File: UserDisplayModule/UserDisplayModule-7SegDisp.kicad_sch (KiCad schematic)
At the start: 15 parts, among them U4 74HC595

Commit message: doubled LEDs + started PCB
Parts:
- removed D13: 1SEG7, symbol Device:LED
- removed D14: 1SEG6, symbol Device:LED
- removed D15: 1SEG5, symbol Device:LED
- removed D16: 1SEG4, symbol Device:LED
- removed D17: 1SEG3, symbol Device:LED
- removed D18: 1SEG2, symbol Device:LED
- removed D19: 1SEG1, symbol Device:LED
- added D27: SEG7, LED_SMD:LED_0805_2012Metric, symbol Device:LED
- added D28, D30, D32, D34, D36, D38, D40: BAT1, LED_SMD:LED_0805_2012Metric, symbol Device:LED
- added D29: SEG6, LED_SMD:LED_0805_2012Metric, symbol Device:LED
- added D31: SEG5, LED_SMD:LED_0805_2012Metric, symbol Device:LED
- added D33: SEG4, LED_SMD:LED_0805_2012Metric, symbol Device:LED
- added D35: SEG3, LED_SMD:LED_0805_2012Metric, symbol Device:LED
- added D37: SEG2, LED_SMD:LED_0805_2012Metric, symbol Device:LED
- added D39: SEG1, LED_SMD:LED_0805_2012Metric, symbol Device:LED
- R13, R14, R15, R16, R17, R18, R19: footprint (none) -> Resistor_SMD:R_0805_2012Metric
- U4: footprint (none) -> ImportedFootprints:CD74HC595E
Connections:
- net GND: now also D28.1 (K), D30.1 (K), D32.1 (K), D34.1 (K), D36.1 (K), D38.1 (K), D40.1 (K)
- net at R14.2: now also D29.2 (A)
- net at R13.2: now also D27.2 (A)
- net at R15.2: now also D31.2 (A)
- net at R19.2: now also D39.2 (A)
- net at R16.2: now also D33.2 (A)
- net at R18.2: now also D37.2 (A)
- net at R17.2: now also D35.2 (A)
- new net: D29.1 (K), D30.2 (A)
- new net: D31.1 (K), D32.2 (A)
- new net: D37.1 (K), D38.2 (A)
- new net: D27.1 (K), D28.2 (A)
- new net: D39.1 (K), D40.2 (A)
- new net: D35.1 (K), D36.2 (A)
- new net: D33.1 (K), D34.2 (A)
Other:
- note added: "7-Segment Display"
- moved on the sheet: R13, R14, R15, R16, R17, R18, R19

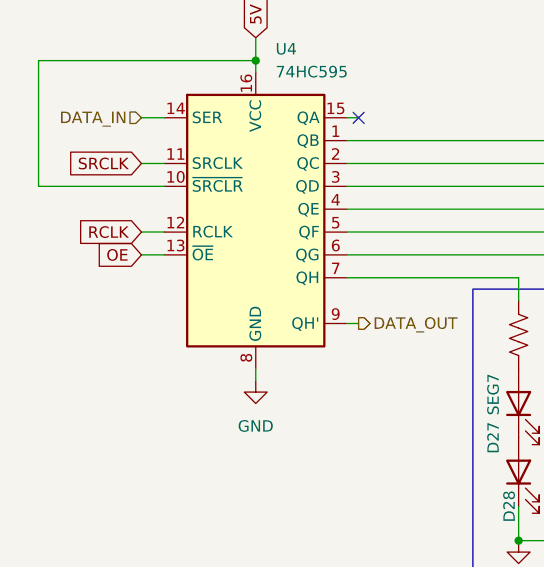
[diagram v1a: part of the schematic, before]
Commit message: finished routing pcb (minus ground pour)
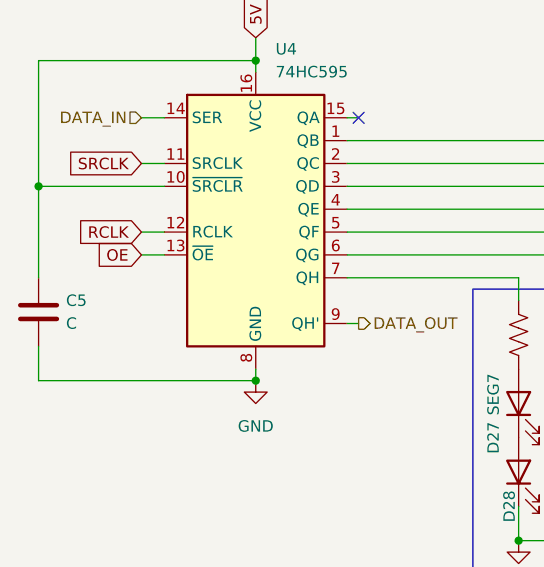
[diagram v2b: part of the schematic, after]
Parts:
- added C5: C, Capacitor_SMD:C_0805_2012Metric, symbol Device:C
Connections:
- net 5V: now also C5.1
- net GND: now also C5.2
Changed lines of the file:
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@@
+	)
+	(junction
+		(at 78.74 62.23)
+		(diameter 0)
+		(color 0 0 0 0)
 	)
 	(junction
@@
 	)
 	(junction
+		(at 102.87 83.82)
+		(diameter 0)
+		(color 0 0 0 0)
+	)
+	(junction
 		(at 132.08 101.6)
 		(diameter 0)
@@
 	(wire
 		(pts
+			(xy 78.74 62.23) (xy 78.74 72.39)
+		)
+		(stroke
+			(width 0)
+			(type default)
+		)
+	)
+	(wire
+		(pts
 			(xy 113.03 54.61) (xy 114.3 54.61)
 		)
@@
 	(wire
 		(pts
+			(xy 78.74 83.82) (xy 102.87 83.82)
+		)
+		(stroke
+			(width 0)
+			(type default)
+		)
+	)
+	(wire
+		(pts
 			(xy 113.03 62.23) (xy 187.96 62.23)
 		)
@@
 		(pts
 			(xy 113.03 57.15) (xy 215.9 57.15)
+		)
+		(stroke
+			(width 0)
+			(type default)
+		)
+	)
+	(wire
+		(pts
+			(xy 78.74 80.01) (xy 78.74 83.82)
 		)
 		(stroke
@@
 					(unit 1)
 				)
+			)
+		)
+	)
+	(symbol
+		(lib_id "Device:C")
+		(at 78.74 76.2 0)
+		(unit 1)
+		(exclude_from_sim no)
+		(in_bom yes)
+		(on_board yes)
+		(dnp no)
+		(property "Reference" "C5"
+			(at 81.788 74.93 0)
+			(effects
+				(font
+					(size 1.27 1.27)
+				)
+				(justify left)
+			)
+		)
+		(property "Value" "C"
+			(at 81.788 77.47 0)
+			(effects
+				(font
+					(size 1.27 1.27)
+				)
+				(justify left)
+			)
+		)
+		(property "Footprint" "Capacitor_SMD:C_0805_2012Metric"
+			(at 79.7052 80.01 0)
+			(effects
+				(font
+					(size 1.27 1.27)
+				)
+				(hide yes)
+			)
+		)
+		(property "Datasheet" "~"
+			(at 78.74 76.2 0)
+			(effects
+				(font
+					(size 1.27 1.27)
+				)
+				(hide yes)
+			)
+		)
+		(property "Description" "Unpolarized capacitor"
+			(at 78.74 76.2 0)
+			(effects
+				(font
+					(size 1.27 1.27)
+				)
+				(hide yes)
+			)
+		)
+		(pin "2"
+		)
+		(pin "1"
+		)
+		(instances
+			(project "UserDisplayModule"
+				(path "/352d7abe-fc72-4473-8b68-62eecf44f496/0028eded-db04-4ec8-8943-95ff11960fa1"
+					(reference "C5")
+					(unit 1)
+				)
+				(path "/352d7abe-fc72-4473-8b68-62eecf44f496/d2d9e71a-442b-4090-b915-11a66e8f5c2a"
+					(reference "C6")
+					(unit 1)
+				)
+				(path "/352d7abe-fc72-4473-8b68-62eecf44f496/9650799d-9072-4dba-8139-3ec1f2ecacfb"
+					(reference "C7")
+					(unit 1)
+				)
+				(path "/352d7abe-fc72-4473-8b68-62eecf44f496/b2dcfe67-b35c-4587-a29d-880113cdb577"
+					(reference "C8")
+					(unit 1)
+				)

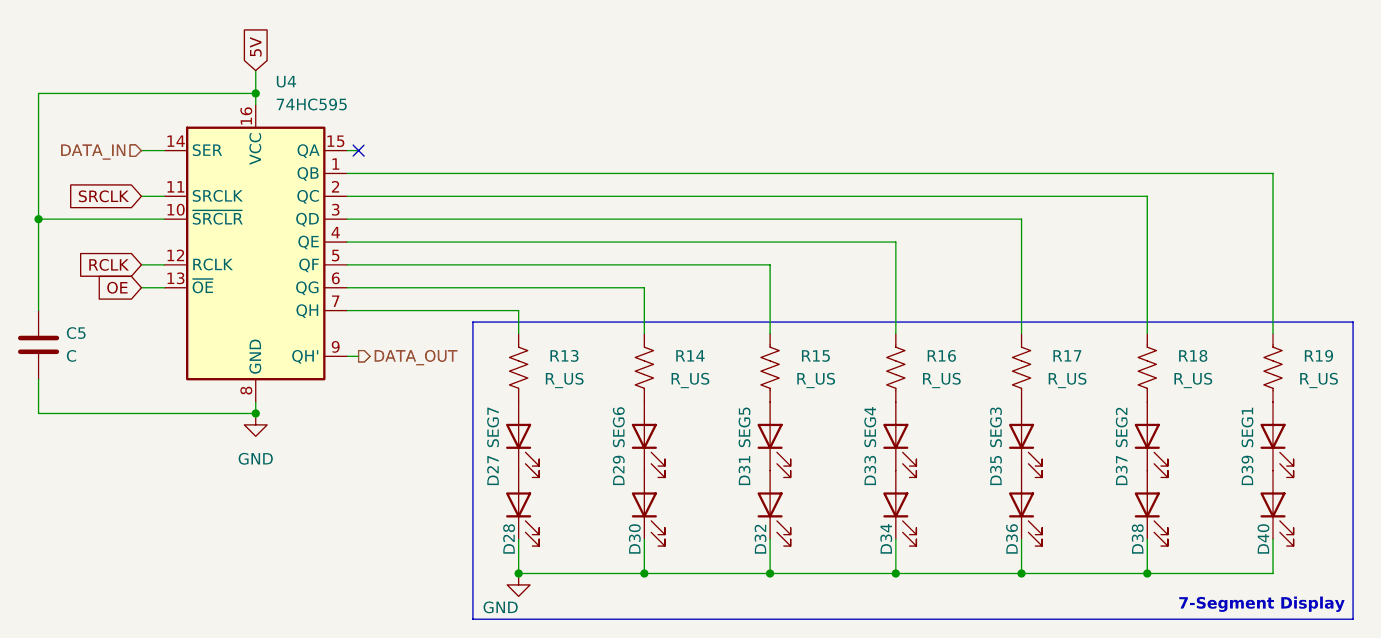
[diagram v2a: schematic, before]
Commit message: added 3d models, fixed footprints, finished routing
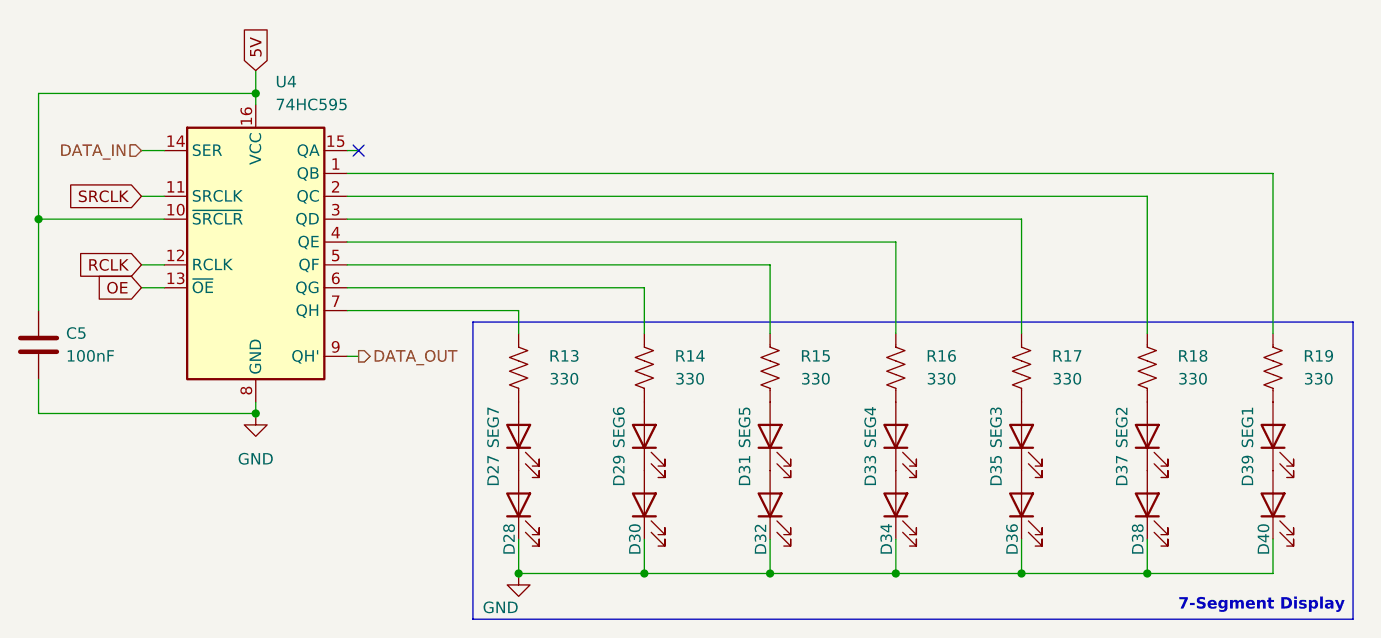
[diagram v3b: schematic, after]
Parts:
- C5: value C -> 100nF
- R13, R14, R15, R16, R17, R18, R19: value R_US -> 330
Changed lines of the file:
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@@
 			)
 		)
-		(property "Value" "R_US"
+		(property "Value" "330"
 			(at 151.13 80.01 0)
 			(effects
@@
 			)
 		)
-		(property "Value" "R_US"
+		(property "Value" "330"
 			(at 137.16 80.01 0)
 			(effects
@@
 			)
 		)
-		(property "Value" "R_US"
+		(property "Value" "330"
 			(at 165.1 80.01 0)
 			(effects
@@
 			)
 		)
-		(property "Value" "R_US"
+		(property "Value" "330"
 			(at 220.98 80.01 0)
 			(effects
@@
 			)
 		)
-		(property "Value" "R_US"
+		(property "Value" "330"
 			(at 179.07 80.01 0)
 			(effects
@@
 			)
 		)
-		(property "Value" "R_US"
+		(property "Value" "330"
 			(at 207.01 80.01 0)
 			(effects
@@
 			)
 		)
-		(property "Value" "R_US"
+		(property "Value" "330"
 			(at 193.04 80.01 0)
 			(effects
@@
 			)
 		)
-		(property "Value" "C"
+		(property "Value" "100nF"
 			(at 81.788 77.47 0)
 			(effects

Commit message: added digikey pns
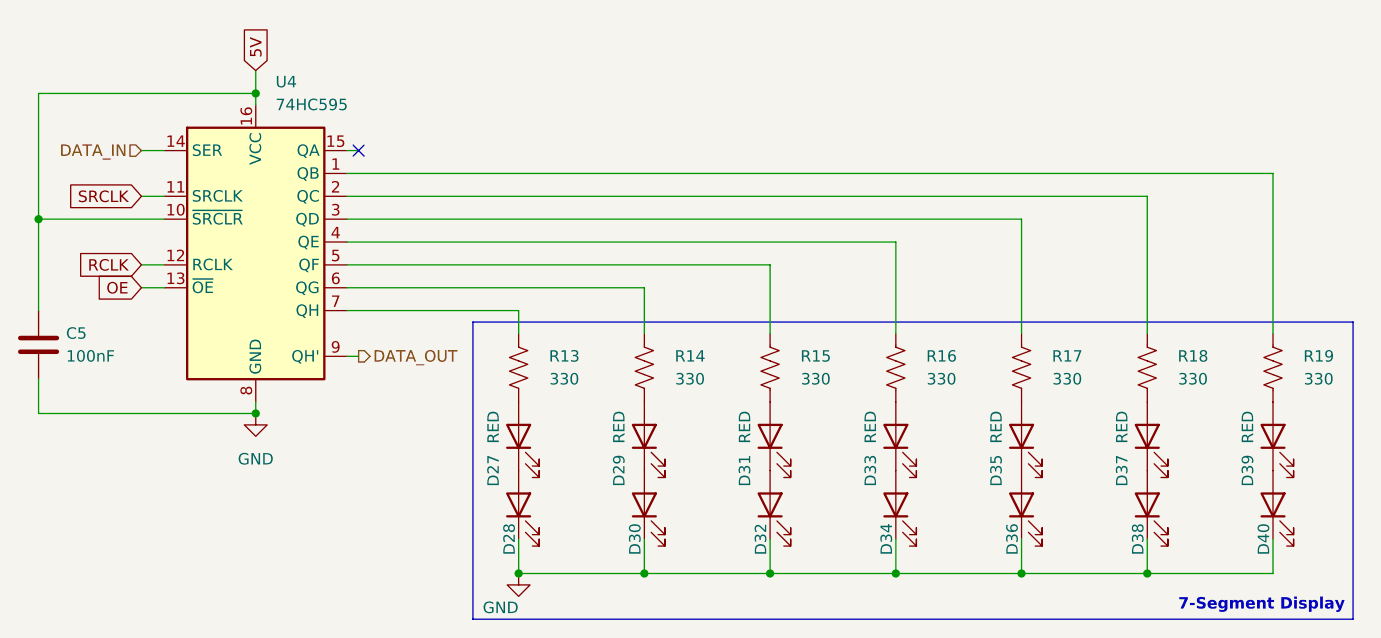
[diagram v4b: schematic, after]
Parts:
- D27: value SEG7 -> RED; Digikey PN (none) -> 732-4984-1-ND
- D28, D30, D32, D34, D36, D38, D40: value BAT1 -> RED; Digikey PN (none) -> 732-4984-1-ND
- D29: value SEG6 -> RED; Digikey PN (none) -> 732-4984-1-ND
- D31: value SEG5 -> RED; Digikey PN (none) -> 732-4984-1-ND
- D33: value SEG4 -> RED; Digikey PN (none) -> 732-4984-1-ND
- D35: value SEG3 -> RED; Digikey PN (none) -> 732-4984-1-ND
- D37: value SEG2 -> RED; Digikey PN (none) -> 732-4984-1-ND
- D39: value SEG1 -> RED; Digikey PN (none) -> 732-4984-1-ND
- U4: Digikey PN (none) -> 296-1600-5-ND
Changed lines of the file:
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@@
 			)
 		)
-		(property "Value" "BAT1"
+		(property "Value" "RED"
 			(at 152.0825 97.155 90)
 			(effects
@@
 			)
 		)
+		(property "Digikey PN" "732-4984-1-ND"
+			(at 146.05 93.98 0)
+			(effects
+				(font
+					(size 1.27 1.27)
+				)
+				(hide yes)
+			)
+		)
 		(pin "1"
 		)
@@
 			)
 		)
+		(property "Digikey PN" ""
+			(at 146.05 78.74 0)
+			(effects
+				(font
+					(size 1.27 1.27)
+				)
+				(hide yes)
+			)
+		)
 		(pin "1"
 		)
@@
 			)
 		)
-		(property "Value" "SEG5"
+		(property "Value" "RED"
 			(at 157.226 85.344 0)
 			(effects
@@
 			)
 		)
+		(property "Digikey PN" "732-4984-1-ND"
+			(at 160.02 86.36 0)
+			(effects
+				(font
+					(size 1.27 1.27)
+				)
+				(hide yes)
+			)
+		)
 		(pin "1"
 		)
@@
 			)
 		)
-		(property "Value" "SEG2"
+		(property "Value" "RED"
 			(at 199.136 85.344 0)
 			(effects
@@
 			)
 		)
+		(property "Digikey PN" "732-4984-1-ND"
+			(at 201.93 86.36 0)
+			(effects
+				(font
+					(size 1.27 1.27)
+				)
+				(hide yes)
+			)
+		)
 		(pin "1"
 		)
@@
 			)
 		)
-		(property "Value" "SEG7"
+		(property "Value" "RED"
 			(at 129.286 85.344 0)
 			(effects
@@
 			)
 		)
+		(property "Digikey PN" "732-4984-1-ND"
+			(at 132.08 86.36 0)
+			(effects
+				(font
+					(size 1.27 1.27)
+				)
+				(hide yes)
+			)
+		)
 		(pin "1"
 		)
@@
 			)
 		)
+		(property "Digikey PN" ""
+			(at 132.08 78.74 0)
+			(effects
+				(font
+					(size 1.27 1.27)
+				)
+				(hide yes)
+			)
+		)
 		(pin "1"
 		)
@@
 			)
 		)
-		(property "Value" "BAT1"
+		(property "Value" "RED"
 			(at 207.9625 97.155 90)
 			(effects
@@
 		)
 		(property "Description" "Light emitting diode"
+			(at 201.93 93.98 0)
+			(effects
+				(font
+					(size 1.27 1.27)
+				)
+				(hide yes)
+			)
+		)
+		(property "Digikey PN" "732-4984-1-ND"
 			(at 201.93 93.98 0)
 			(effects
@@
 			)
 		)
-		(property "Value" "SEG6"
+		(property "Value" "RED"
 			(at 143.256 85.344 0)
 			(effects
@@
 			)
 		)
+		(property "Digikey PN" "732-4984-1-ND"
+			(at 146.05 86.36 0)
+			(effects
+				(font
+					(size 1.27 1.27)
+				)
+				(hide yes)
+			)
+		)
 		(pin "1"
 		)
@@
 			)
 		)
-		(property "Value" "BAT1"
+		(property "Value" "RED"
 			(at 221.9325 97.155 90)
 			(effects
@@
 			)
 		)
+		(property "Digikey PN" "732-4984-1-ND"
+			(at 215.9 93.98 0)
+			(effects
+				(font
+					(size 1.27 1.27)
+				)
+				(hide yes)
+			)
+		)
 		(pin "1"
 		)
@@
 			)
 		)
-		(property "Value" "BAT1"
+		(property "Value" "RED"
 			(at 166.0525 97.155 90)
 			(effects
@@
 			)
 		)
+		(property "Digikey PN" "732-4984-1-ND"
+			(at 160.02 93.98 0)
+			(effects
+				(font
+					(size 1.27 1.27)
+				)
+				(hide yes)
+			)
+		)
 		(pin "1"
 		)
@@
 			)
 		)
+		(property "Digikey PN" ""
+			(at 160.02 78.74 0)
+			(effects
+				(font
+					(size 1.27 1.27)
+				)
+				(hide yes)
+			)
+		)
 		(pin "1"
 		)
@@
 			)
 		)
+		(property "Digikey PN" ""
+			(at 215.9 78.74 0)
+			(effects
+				(font
+					(size 1.27 1.27)
+				)
+				(hide yes)
+			)
+		)
 		(pin "1"
 		)
@@
 			)
 		)
+		(property "Digikey PN" ""
+			(at 173.99 78.74 0)
+			(effects
+				(font
+					(size 1.27 1.27)
+				)
+				(hide yes)
+			)
+		)
 		(pin "1"
 		)
@@
 			)
 		)
-		(property "Value" "BAT1"
+		(property "Value" "RED"
 			(at 193.9925 97.155 90)
 			(effects
@@
 			)
 		)
+		(property "Digikey PN" "732-4984-1-ND"
+			(at 187.96 93.98 0)
+			(effects
+				(font
+					(size 1.27 1.27)
+				)
+				(hide yes)
+			)
+		)
 		(pin "1"
 		)
@@
 		)
 		(property "Description" "Resistor, US symbol"
+			(at 201.93 78.74 0)
+			(effects
+				(font
+					(size 1.27 1.27)
+				)
+				(hide yes)
+			)
+		)
+		(property "Digikey PN" ""
 			(at 201.93 78.74 0)
 			(effects
@@
 			)
 		)
+		(property "Digikey PN" "296-1600-5-ND"
+			(at 102.87 64.77 0)
+			(effects
+				(font
+					(size 1.27 1.27)
+				)
+				(hide yes)
+			)
+		)
 		(pin "9"
 		)
@@
 			)
 		)
-		(property "Value" "SEG1"
+		(property "Value" "RED"
 			(at 213.106 85.344 0)
 			(effects
@@
 			)
 		)
+		(property "Digikey PN" "732-4984-1-ND"
+			(at 215.9 86.36 0)
+			(effects
+				(font
+					(size 1.27 1.27)
+				)
+				(hide yes)
+			)
+		)
 		(pin "1"
 		)
@@
 			)
 		)
-		(property "Value" "BAT1"
+		(property "Value" "RED"
 			(at 180.0225 97.155 90)
 			(effects
@@
 			)
 		)
+		(property "Digikey PN" "732-4984-1-ND"
+			(at 173.99 93.98 0)
+			(effects
+				(font
+					(size 1.27 1.27)
+				)
+				(hide yes)
+			)
+		)
 		(pin "1"
 		)
@@
 			)
 		)
+		(property "Digikey PN" ""
+			(at 187.96 78.74 0)
+			(effects
+				(font
+					(size 1.27 1.27)
+				)
+				(hide yes)
+			)
+		)
 		(pin "1"
 		)
@@
 			)
 		)
+		(property "Digikey PN" ""
+			(at 78.74 76.2 0)
+			(effects
+				(font
+					(size 1.27 1.27)
+				)
+				(hide yes)
+			)
+		)
 		(pin "2"
 		)
@@
 			)
 		)
-		(property "Value" "SEG3"
+		(property "Value" "RED"
 			(at 185.166 85.344 0)
 			(effects
@@
 			)
 		)
+		(property "Digikey PN" "732-4984-1-ND"
+			(at 187.96 86.36 0)
+			(effects
+				(font
+					(size 1.27 1.27)
+				)
+				(hide yes)
+			)
+		)
 		(pin "1"
 		)
@@
 			)
 		)
-		(property "Value" "BAT1"
+		(property "Value" "RED"
 			(at 138.1125 97.155 90)
 			(effects
@@
 			)
 		)
+		(property "Digikey PN" "732-4984-1-ND"
+			(at 132.08 93.98 0)
+			(effects
+				(font
+					(size 1.27 1.27)
+				)
+				(hide yes)
+			)
+		)
 		(pin "1"
 		)
@@
 			)
 		)
-		(property "Value" "SEG4"
+		(property "Value" "RED"
 			(at 171.196 85.344 0)
 			(effects
@@
 			(at 173.99 86.36 0)
 			(effects
+				(font
+					(size 1.27 1.27)
+				)
+				(hide yes)
+			)
+		)
+		(property "Digikey PN" "732-4984-1-ND"
+			(at 173.99 86.36 0)
+			(effects

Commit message: Edited BOM for R/C parts
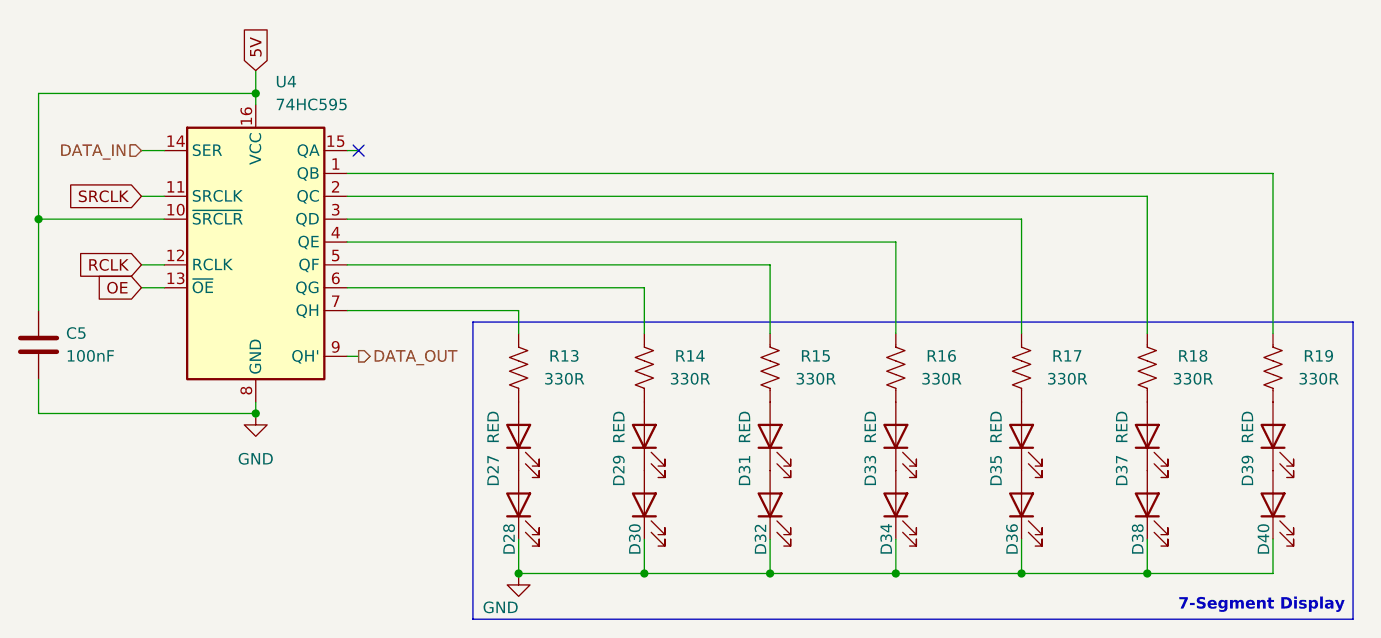
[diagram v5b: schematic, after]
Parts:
- C5: Digikey PN (none) -> 1276-1003-1-ND
- R13, R14, R15, R16, R17, R18, R19: value 330 -> 330R; Digikey PN (none) -> RMCF0805FT330RCT-ND
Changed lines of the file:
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@@
 			)
 		)
-		(property "Value" "330"
+		(property "Value" "330R"
 			(at 151.13 80.01 0)
 			(effects
@@
 			)
 		)
-		(property "Digikey PN" ""
+		(property "Digikey PN" "RMCF0805FT330RCT-ND"
 			(at 146.05 78.74 0)
 			(effects
@@
 			)
 		)
-		(property "Value" "330"
+		(property "Value" "330R"
 			(at 137.16 80.01 0)
 			(effects
@@
 			)
 		)
-		(property "Digikey PN" ""
+		(property "Digikey PN" "RMCF0805FT330RCT-ND"
 			(at 132.08 78.74 0)
 			(effects
@@
 			)
 		)
-		(property "Value" "330"
+		(property "Value" "330R"
 			(at 165.1 80.01 0)
 			(effects
@@
 			)
 		)
-		(property "Digikey PN" ""
+		(property "Digikey PN" "RMCF0805FT330RCT-ND"
 			(at 160.02 78.74 0)
 			(effects
@@
 			)
 		)
-		(property "Value" "330"
+		(property "Value" "330R"
 			(at 220.98 80.01 0)
 			(effects
@@
 			)
 		)
-		(property "Digikey PN" ""
+		(property "Digikey PN" "RMCF0805FT330RCT-ND"
 			(at 215.9 78.74 0)
 			(effects
@@
 			)
 		)
-		(property "Value" "330"
+		(property "Value" "330R"
 			(at 179.07 80.01 0)
 			(effects
@@
 			)
 		)
-		(property "Digikey PN" ""
+		(property "Digikey PN" "RMCF0805FT330RCT-ND"
 			(at 173.99 78.74 0)
 			(effects
@@
 			)
 		)
-		(property "Value" "330"
+		(property "Value" "330R"
 			(at 207.01 80.01 0)
 			(effects
@@
 			)
 		)
-		(property "Digikey PN" ""
+		(property "Digikey PN" "RMCF0805FT330RCT-ND"
 			(at 201.93 78.74 0)
 			(effects
@@
 			)
 		)
-		(property "Value" "330"
+		(property "Value" "330R"
 			(at 193.04 80.01 0)
 			(effects
@@
 			)
 		)
-		(property "Digikey PN" ""
+		(property "Digikey PN" "RMCF0805FT330RCT-ND"
 			(at 187.96 78.74 0)
 			(effects
@@
 			)
 		)
-		(property "Digikey PN" ""
+		(property "Digikey PN" "1276-1003-1-ND"
 			(at 78.74 76.2 0)
 			(effects
